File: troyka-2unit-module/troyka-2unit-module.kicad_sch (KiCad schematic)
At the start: 4 parts, among them J1 UP (A), J2 DOWN (A)

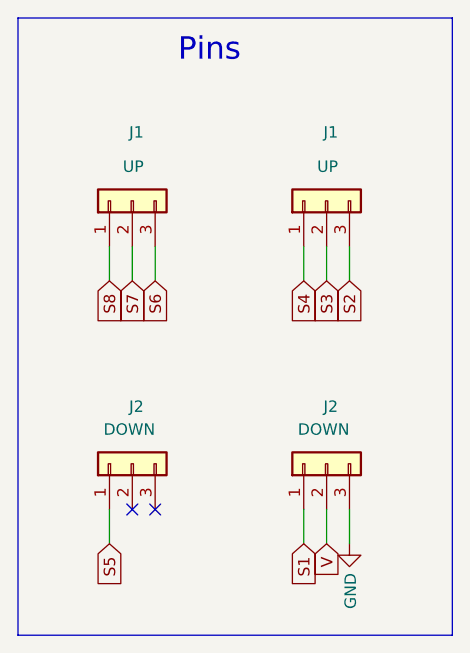
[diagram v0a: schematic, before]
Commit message: Update templates and CI
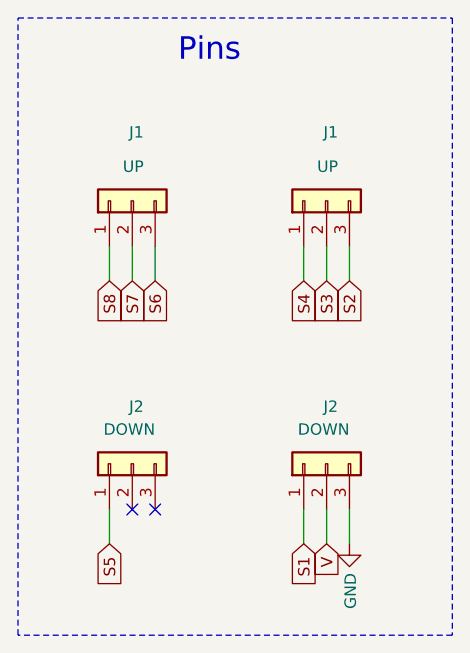
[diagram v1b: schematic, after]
